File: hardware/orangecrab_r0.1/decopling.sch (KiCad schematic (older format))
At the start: 22 parts

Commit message: Completed 99% of routing.
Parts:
- added C74: 10n, Capacitor_SMD:C_0201_0603Metric, symbol Device:C
- added C75: 100n, Capacitor_SMD:C_0201_0603Metric, symbol Device:C
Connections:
- net GND: now also C74.2, C75.2
- net P3.3V: now also C74.1, C75.1
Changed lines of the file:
@@
 Wire Wire Line
 	4700 4000 4700 4050
+$Comp
+L Device:C C74
+U 1 1 5D761CBE
+P 5600 3800
+F 0 "C74" H 5485 3846 50  0000 R CNN
+F 1 "10n" H 5485 3755 50  0000 R CNN
+F 2 "Capacitor_SMD:C_0201_0603Metric" H 5638 3650 50  0001 C CNN
+F 3 "~" H 5600 3800 50  0001 C CNN
+	1    5600 3800
+	1    0    0    -1
+$EndComp
+$Comp
+L gkl_power:GND #PWR0163
+U 1 1 5D761CC8
+P 5600 4050
+F 0 "#PWR0163" H 5600 3800 50  0001 C CNN
+F 1 "GND" H 5603 3924 50  0000 C CNN
+F 2 "" H 5500 3700 50  0001 C CNN
+F 3 "" H 5600 4050 50  0001 C CNN
+	1    5600 4050
+	1    0    0    -1
+$EndComp
+$Comp
+L Device:C C75
+U 1 1 5D761CD2
+P 5800 3800
+F 0 "C75" H 5915 3846 50  0000 L CNN
+F 1 "100n" H 5915 3755 50  0000 L CNN
+F 2 "Capacitor_SMD:C_0201_0603Metric" H 5838 3650 50  0001 C CNN
+F 3 "~" H 5800 3800 50  0001 C CNN
+	1    5800 3800
+	1    0    0    -1
+$EndComp
+Text GLabel 5800 3550 1    50   UnSpc ~ 0
+P3.3V
+Wire Wire Line
+	5600 3650 5600 3600
+Wire Wire Line
+	5600 3600 5800 3600
+Wire Wire Line
+	5800 3600 5800 3550
+Wire Wire Line
+	5800 3650 5800 3600
+Connection ~ 5800 3600
+Wire Wire Line
+	5600 3950 5600 4000
+Wire Wire Line
+	5600 4000 5800 4000
+Wire Wire Line
+	5800 4000 5800 3950
+Connection ~ 5600 4000
+Wire Wire Line
+	5600 4000 5600 4050
 $EndSCHEMATC

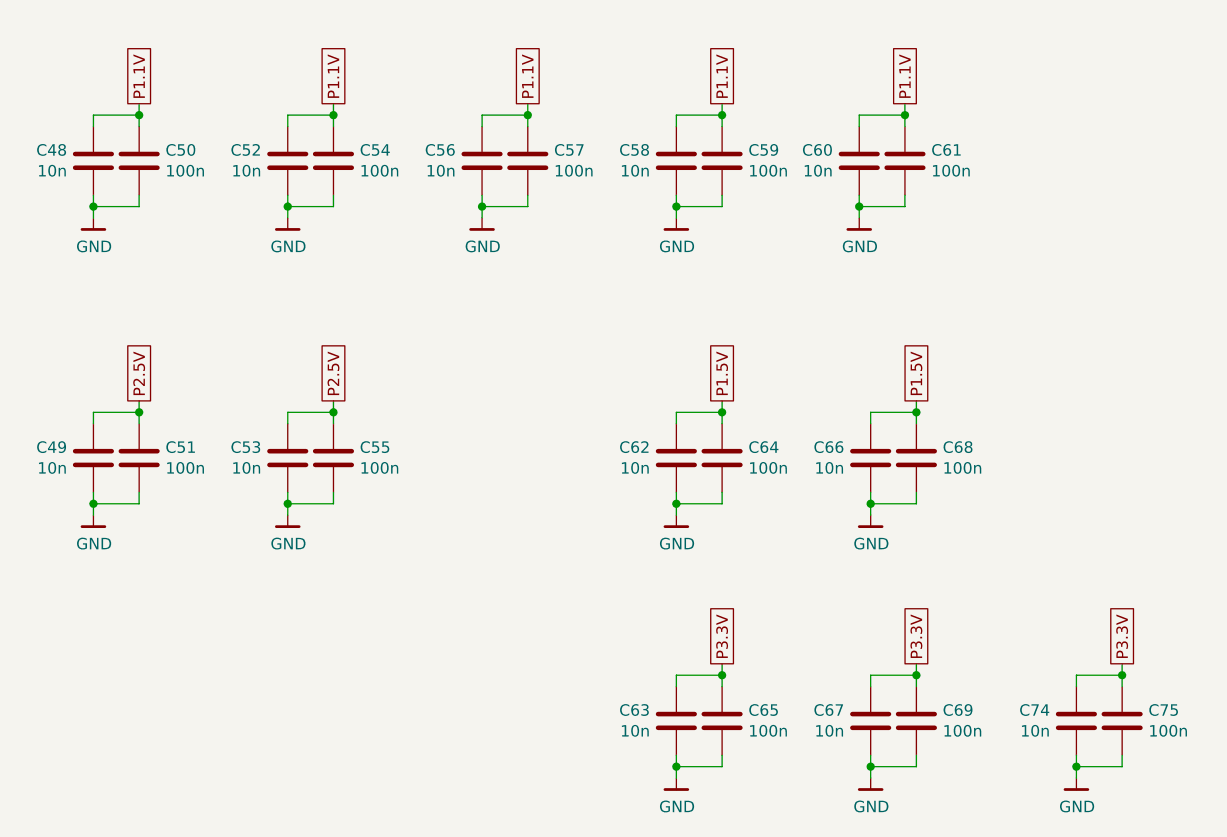
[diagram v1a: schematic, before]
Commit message: Added pulldown on TS pin to disable TS func. Added 4.7uF cap to USB input. Corrected Battery polarity Calculated correct DCDC Fb Added pullup to SWCLK Added Pulldown to TCK Added Pinout legend on top layer Fixed Missing VCC on Flash Neaten up Power Plane Schematic Checklist complete.
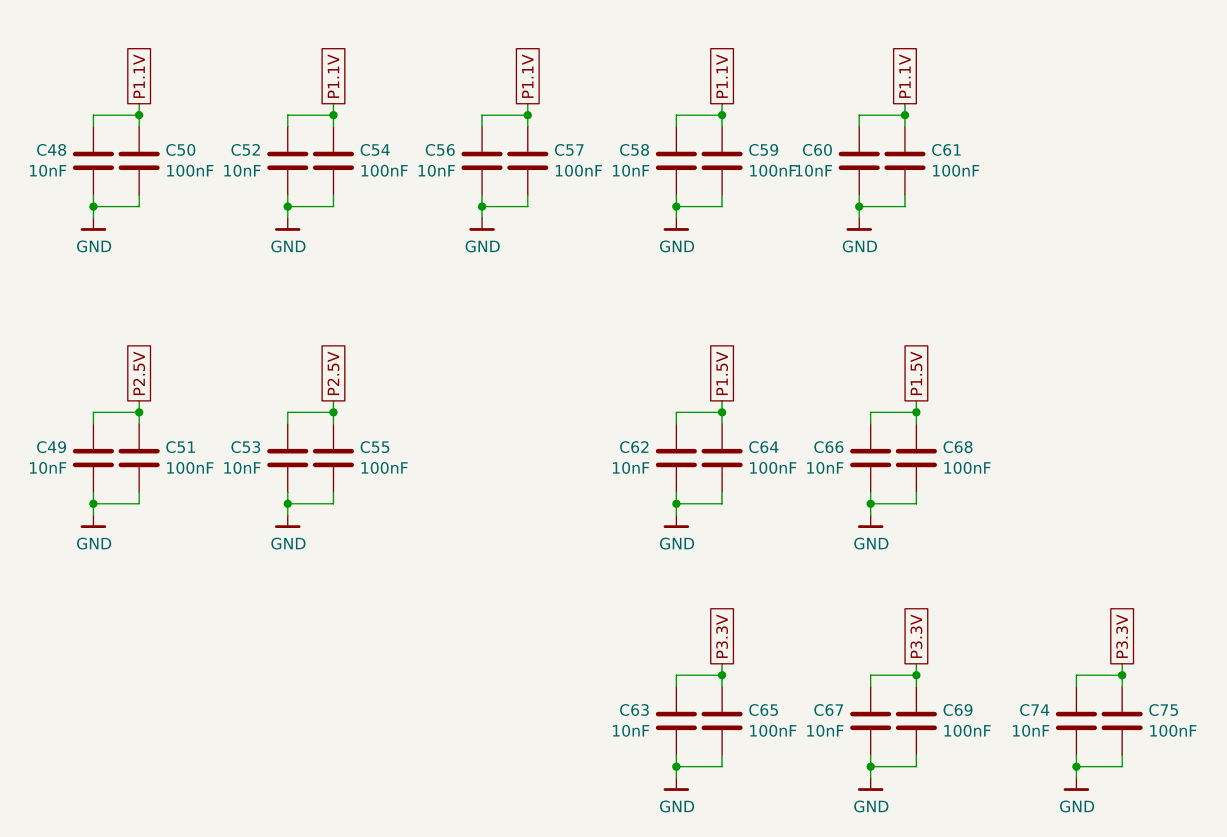
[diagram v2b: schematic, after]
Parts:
- C48, C49, C52, C53, C56, C58, C60, C62, C63, C66, C67, C74: value 10n -> 10nF
- C50, C51, C54, C55, C57, C59, C61, C64, C65, C68, C69, C75: value 100n -> 100nF
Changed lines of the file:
@@
 P 1300 1350
 F 0 "C48" H 1185 1396 50  0000 R CNN
-F 1 "10n" H 1185 1305 50  0000 R CNN
+F 1 "10nF" H 1185 1305 50  0000 R CNN
 F 2 "Capacitor_SMD:C_0201_0603Metric" H 1338 1200 50  0001 C CNN
 F 3 "~" H 1300 1350 50  0001 C CNN
@@
 P 1500 1350
 F 0 "C50" H 1615 1396 50  0000 L CNN
-F 1 "100n" H 1615 1305 50  0000 L CNN
+F 1 "100nF" H 1615 1305 50  0000 L CNN
 F 2 "Capacitor_SMD:C_0201_0603Metric" H 1538 1200 50  0001 C CNN
 F 3 "~" H 1500 1350 50  0001 C CNN
@@
 P 2150 1350
 F 0 "C52" H 2035 1396 50  0000 R CNN
-F 1 "10n" H 2035 1305 50  0000 R CNN
+F 1 "10nF" H 2035 1305 50  0000 R CNN
 F 2 "Capacitor_SMD:C_0201_0603Metric" H 2188 1200 50  0001 C CNN
 F 3 "~" H 2150 1350 50  0001 C CNN
@@
 P 2350 1350
 F 0 "C54" H 2465 1396 50  0000 L CNN
-F 1 "100n" H 2465 1305 50  0000 L CNN
+F 1 "100nF" H 2465 1305 50  0000 L CNN
 F 2 "Capacitor_SMD:C_0201_0603Metric" H 2388 1200 50  0001 C CNN
 F 3 "~" H 2350 1350 50  0001 C CNN
@@
 P 3000 1350
 F 0 "C56" H 2885 1396 50  0000 R CNN
-F 1 "10n" H 2885 1305 50  0000 R CNN
+F 1 "10nF" H 2885 1305 50  0000 R CNN
 F 2 "Capacitor_SMD:C_0201_0603Metric" H 3038 1200 50  0001 C CNN
 F 3 "~" H 3000 1350 50  0001 C CNN
@@
 P 3200 1350
 F 0 "C57" H 3315 1396 50  0000 L CNN
-F 1 "100n" H 3315 1305 50  0000 L CNN
+F 1 "100nF" H 3315 1305 50  0000 L CNN
 F 2 "Capacitor_SMD:C_0201_0603Metric" H 3238 1200 50  0001 C CNN
 F 3 "~" H 3200 1350 50  0001 C CNN
@@
 P 3850 1350
 F 0 "C58" H 3735 1396 50  0000 R CNN
-F 1 "10n" H 3735 1305 50  0000 R CNN
+F 1 "10nF" H 3735 1305 50  0000 R CNN
 F 2 "Capacitor_SMD:C_0201_0603Metric" H 3888 1200 50  0001 C CNN
 F 3 "~" H 3850 1350 50  0001 C CNN
@@
 P 4050 1350
 F 0 "C59" H 4165 1396 50  0000 L CNN
-F 1 "100n" H 4165 1305 50  0000 L CNN
+F 1 "100nF" H 4165 1305 50  0000 L CNN
 F 2 "Capacitor_SMD:C_0201_0603Metric" H 4088 1200 50  0001 C CNN
 F 3 "~" H 4050 1350 50  0001 C CNN
@@
 P 4650 1350
 F 0 "C60" H 4535 1396 50  0000 R CNN
-F 1 "10n" H 4535 1305 50  0000 R CNN
+F 1 "10nF" H 4535 1305 50  0000 R CNN
 F 2 "Capacitor_SMD:C_0201_0603Metric" H 4688 1200 50  0001 C CNN
 F 3 "~" H 4650 1350 50  0001 C CNN
@@
 P 4850 1350
 F 0 "C61" H 4965 1396 50  0000 L CNN
-F 1 "100n" H 4965 1305 50  0000 L CNN
+F 1 "100nF" H 4965 1305 50  0000 L CNN
 F 2 "Capacitor_SMD:C_0201_0603Metric" H 4888 1200 50  0001 C CNN
 F 3 "~" H 4850 1350 50  0001 C CNN
@@
 P 1300 2650
 F 0 "C49" H 1185 2696 50  0000 R CNN
-F 1 "10n" H 1185 2605 50  0000 R CNN
+F 1 "10nF" H 1185 2605 50  0000 R CNN
 F 2 "Capacitor_SMD:C_0201_0603Metric" H 1338 2500 50  0001 C CNN
 F 3 "~" H 1300 2650 50  0001 C CNN
@@
 P 1500 2650
 F 0 "C51" H 1615 2696 50  0000 L CNN
-F 1 "100n" H 1615 2605 50  0000 L CNN
+F 1 "100nF" H 1615 2605 50  0000 L CNN
 F 2 "Capacitor_SMD:C_0201_0603Metric" H 1538 2500 50  0001 C CNN
 F 3 "~" H 1500 2650 50  0001 C CNN
@@
 P 2150 2650
 F 0 "C53" H 2035 2696 50  0000 R CNN
-F 1 "10n" H 2035 2605 50  0000 R CNN
+F 1 "10nF" H 2035 2605 50  0000 R CNN
 F 2 "Capacitor_SMD:C_0201_0603Metric" H 2188 2500 50  0001 C CNN
 F 3 "~" H 2150 2650 50  0001 C CNN
@@
 P 2350 2650
 F 0 "C55" H 2465 2696 50  0000 L CNN
-F 1 "100n" H 2465 2605 50  0000 L CNN
+F 1 "100nF" H 2465 2605 50  0000 L CNN
 F 2 "Capacitor_SMD:C_0201_0603Metric" H 2388 2500 50  0001 C CNN
 F 3 "~" H 2350 2650 50  0001 C CNN
@@
 P 3850 2650
 F 0 "C62" H 3735 2696 50  0000 R CNN
-F 1 "10n" H 3735 2605 50  0000 R CNN
+F 1 "10nF" H 3735 2605 50  0000 R CNN
 F 2 "Capacitor_SMD:C_0201_0603Metric" H 3888 2500 50  0001 C CNN
 F 3 "~" H 3850 2650 50  0001 C CNN
@@
 P 4050 2650
 F 0 "C64" H 4165 2696 50  0000 L CNN
-F 1 "100n" H 4165 2605 50  0000 L CNN
+F 1 "100nF" H 4165 2605 50  0000 L CNN
 F 2 "Capacitor_SMD:C_0201_0603Metric" H 4088 2500 50  0001 C CNN
 F 3 "~" H 4050 2650 50  0001 C CNN
@@
 P 4700 2650
 F 0 "C66" H 4585 2696 50  0000 R CNN
-F 1 "10n" H 4585 2605 50  0000 R CNN
+F 1 "10nF" H 4585 2605 50  0000 R CNN
 F 2 "Capacitor_SMD:C_0201_0603Metric" H 4738 2500 50  0001 C CNN
 F 3 "~" H 4700 2650 50  0001 C CNN
@@
 P 4900 2650
 F 0 "C68" H 5015 2696 50  0000 L CNN
-F 1 "100n" H 5015 2605 50  0000 L CNN
+F 1 "100nF" H 5015 2605 50  0000 L CNN
 F 2 "Capacitor_SMD:C_0201_0603Metric" H 4938 2500 50  0001 C CNN
 F 3 "~" H 4900 2650 50  0001 C CNN
@@
 P 3850 3800
 F 0 "C63" H 3735 3846 50  0000 R CNN
-F 1 "10n" H 3735 3755 50  0000 R CNN
+F 1 "10nF" H 3735 3755 50  0000 R CNN
 F 2 "Capacitor_SMD:C_0201_0603Metric" H 3888 3650 50  0001 C CNN
 F 3 "~" H 3850 3800 50  0001 C CNN
@@
 P 4050 3800
 F 0 "C65" H 4165 3846 50  0000 L CNN
-F 1 "100n" H 4165 3755 50  0000 L CNN
+F 1 "100nF" H 4165 3755 50  0000 L CNN
 F 2 "Capacitor_SMD:C_0201_0603Metric" H 4088 3650 50  0001 C CNN
 F 3 "~" H 4050 3800 50  0001 C CNN
@@
 P 4700 3800
 F 0 "C67" H 4585 3846 50  0000 R CNN
-F 1 "10n" H 4585 3755 50  0000 R CNN
+F 1 "10nF" H 4585 3755 50  0000 R CNN
 F 2 "Capacitor_SMD:C_0201_0603Metric" H 4738 3650 50  0001 C CNN
 F 3 "~" H 4700 3800 50  0001 C CNN
@@
 P 4900 3800
 F 0 "C69" H 5015 3846 50  0000 L CNN
-F 1 "100n" H 5015 3755 50  0000 L CNN
+F 1 "100nF" H 5015 3755 50  0000 L CNN
 F 2 "Capacitor_SMD:C_0201_0603Metric" H 4938 3650 50  0001 C CNN
 F 3 "~" H 4900 3800 50  0001 C CNN
@@
 P 5600 3800
 F 0 "C74" H 5485 3846 50  0000 R CNN
-F 1 "10n" H 5485 3755 50  0000 R CNN
+F 1 "10nF" H 5485 3755 50  0000 R CNN
 F 2 "Capacitor_SMD:C_0201_0603Metric" H 5638 3650 50  0001 C CNN
 F 3 "~" H 5600 3800 50  0001 C CNN
@@
 P 5800 3800
 F 0 "C75" H 5915 3846 50  0000 L CNN
-F 1 "100n" H 5915 3755 50  0000 L CNN
+F 1 "100nF" H 5915 3755 50  0000 L CNN
 F 2 "Capacitor_SMD:C_0201_0603Metric" H 5838 3650 50  0001 C CNN
 F 3 "~" H 5800 3800 50  0001 C CNN

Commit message: Updated BOM fields in KiCad project Exported ibom Clarify fab notes
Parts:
- C48, C49, C52, C53, C56, C58, C60, C62, C63, C66, C67, C74: Mfg (none) -> Samsung Electro-Mechanics; PN (none) -> CL03B103KP3NNNC
- C50, C51, C54, C55, C57, C59, C61, C64, C65, C68, C69, C75: Mfg (none) -> Samsung Electro-Mechanics; PN (none) -> CL03A104KQ3NNNC
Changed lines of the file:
@@
 F 2 "Capacitor_SMD:C_0201_0603Metric" H 1338 1200 50  0001 C CNN
 F 3 "~" H 1300 1350 50  0001 C CNN
+F 4 "Samsung Electro-Mechanics" H 1300 1350 50  0001 C CNN "Mfg"
+F 5 "CL03B103KP3NNNC" H 1300 1350 50  0001 C CNN "PN"
 	1    1300 1350
 	1    0    0    -1
@@
 F 2 "Capacitor_SMD:C_0201_0603Metric" H 1538 1200 50  0001 C CNN
 F 3 "~" H 1500 1350 50  0001 C CNN
+F 4 "Samsung Electro-Mechanics" H 1500 1350 50  0001 C CNN "Mfg"
+F 5 "CL03A104KQ3NNNC" H 1500 1350 50  0001 C CNN "PN"
 	1    1500 1350
 	1    0    0    -1
@@
 F 2 "Capacitor_SMD:C_0201_0603Metric" H 2188 1200 50  0001 C CNN
 F 3 "~" H 2150 1350 50  0001 C CNN
+F 4 "Samsung Electro-Mechanics" H 2150 1350 50  0001 C CNN "Mfg"
+F 5 "CL03B103KP3NNNC" H 2150 1350 50  0001 C CNN "PN"
 	1    2150 1350
 	1    0    0    -1
@@
 F 2 "Capacitor_SMD:C_0201_0603Metric" H 2388 1200 50  0001 C CNN
 F 3 "~" H 2350 1350 50  0001 C CNN
+F 4 "Samsung Electro-Mechanics" H 2350 1350 50  0001 C CNN "Mfg"
+F 5 "CL03A104KQ3NNNC" H 2350 1350 50  0001 C CNN "PN"
 	1    2350 1350
 	1    0    0    -1
@@
 F 2 "Capacitor_SMD:C_0201_0603Metric" H 3038 1200 50  0001 C CNN
 F 3 "~" H 3000 1350 50  0001 C CNN
+F 4 "Samsung Electro-Mechanics" H 3000 1350 50  0001 C CNN "Mfg"
+F 5 "CL03B103KP3NNNC" H 3000 1350 50  0001 C CNN "PN"
 	1    3000 1350
 	1    0    0    -1
@@
 F 2 "Capacitor_SMD:C_0201_0603Metric" H 3238 1200 50  0001 C CNN
 F 3 "~" H 3200 1350 50  0001 C CNN
+F 4 "Samsung Electro-Mechanics" H 3200 1350 50  0001 C CNN "Mfg"
+F 5 "CL03A104KQ3NNNC" H 3200 1350 50  0001 C CNN "PN"
 	1    3200 1350
 	1    0    0    -1
@@
 F 2 "Capacitor_SMD:C_0201_0603Metric" H 3888 1200 50  0001 C CNN
 F 3 "~" H 3850 1350 50  0001 C CNN
+F 4 "Samsung Electro-Mechanics" H 3850 1350 50  0001 C CNN "Mfg"
+F 5 "CL03B103KP3NNNC" H 3850 1350 50  0001 C CNN "PN"
 	1    3850 1350
 	1    0    0    -1
@@
 F 2 "Capacitor_SMD:C_0201_0603Metric" H 4088 1200 50  0001 C CNN
 F 3 "~" H 4050 1350 50  0001 C CNN
+F 4 "Samsung Electro-Mechanics" H 4050 1350 50  0001 C CNN "Mfg"
+F 5 "CL03A104KQ3NNNC" H 4050 1350 50  0001 C CNN "PN"
 	1    4050 1350
 	1    0    0    -1
@@
 F 2 "Capacitor_SMD:C_0201_0603Metric" H 4688 1200 50  0001 C CNN
 F 3 "~" H 4650 1350 50  0001 C CNN
+F 4 "Samsung Electro-Mechanics" H 4650 1350 50  0001 C CNN "Mfg"
+F 5 "CL03B103KP3NNNC" H 4650 1350 50  0001 C CNN "PN"
 	1    4650 1350
 	1    0    0    -1
@@
 F 2 "Capacitor_SMD:C_0201_0603Metric" H 4888 1200 50  0001 C CNN
 F 3 "~" H 4850 1350 50  0001 C CNN
+F 4 "Samsung Electro-Mechanics" H 4850 1350 50  0001 C CNN "Mfg"
+F 5 "CL03A104KQ3NNNC" H 4850 1350 50  0001 C CNN "PN"
 	1    4850 1350
 	1    0    0    -1
@@
 F 2 "Capacitor_SMD:C_0201_0603Metric" H 1338 2500 50  0001 C CNN
 F 3 "~" H 1300 2650 50  0001 C CNN
+F 4 "Samsung Electro-Mechanics" H 1300 2650 50  0001 C CNN "Mfg"
+F 5 "CL03B103KP3NNNC" H 1300 2650 50  0001 C CNN "PN"
 	1    1300 2650
 	1    0    0    -1
@@
 F 2 "Capacitor_SMD:C_0201_0603Metric" H 1538 2500 50  0001 C CNN
 F 3 "~" H 1500 2650 50  0001 C CNN
+F 4 "Samsung Electro-Mechanics" H 1500 2650 50  0001 C CNN "Mfg"
+F 5 "CL03A104KQ3NNNC" H 1500 2650 50  0001 C CNN "PN"
 	1    1500 2650
 	1    0    0    -1
@@
 F 2 "Capacitor_SMD:C_0201_0603Metric" H 2188 2500 50  0001 C CNN
 F 3 "~" H 2150 2650 50  0001 C CNN
+F 4 "Samsung Electro-Mechanics" H 2150 2650 50  0001 C CNN "Mfg"
+F 5 "CL03B103KP3NNNC" H 2150 2650 50  0001 C CNN "PN"
 	1    2150 2650
 	1    0    0    -1
@@
 F 2 "Capacitor_SMD:C_0201_0603Metric" H 2388 2500 50  0001 C CNN
 F 3 "~" H 2350 2650 50  0001 C CNN
+F 4 "Samsung Electro-Mechanics" H 2350 2650 50  0001 C CNN "Mfg"
+F 5 "CL03A104KQ3NNNC" H 2350 2650 50  0001 C CNN "PN"
 	1    2350 2650
 	1    0    0    -1
@@
 F 2 "Capacitor_SMD:C_0201_0603Metric" H 3888 2500 50  0001 C CNN
 F 3 "~" H 3850 2650 50  0001 C CNN
+F 4 "Samsung Electro-Mechanics" H 3850 2650 50  0001 C CNN "Mfg"
+F 5 "CL03B103KP3NNNC" H 3850 2650 50  0001 C CNN "PN"
 	1    3850 2650
 	1    0    0    -1
@@
 F 2 "Capacitor_SMD:C_0201_0603Metric" H 4088 2500 50  0001 C CNN
 F 3 "~" H 4050 2650 50  0001 C CNN
+F 4 "Samsung Electro-Mechanics" H 4050 2650 50  0001 C CNN "Mfg"
+F 5 "CL03A104KQ3NNNC" H 4050 2650 50  0001 C CNN "PN"
 	1    4050 2650
 	1    0    0    -1
@@
 F 2 "Capacitor_SMD:C_0201_0603Metric" H 4738 2500 50  0001 C CNN
 F 3 "~" H 4700 2650 50  0001 C CNN
+F 4 "Samsung Electro-Mechanics" H 4700 2650 50  0001 C CNN "Mfg"
+F 5 "CL03B103KP3NNNC" H 4700 2650 50  0001 C CNN "PN"
 	1    4700 2650
 	1    0    0    -1
@@
 F 2 "Capacitor_SMD:C_0201_0603Metric" H 4938 2500 50  0001 C CNN
 F 3 "~" H 4900 2650 50  0001 C CNN
+F 4 "Samsung Electro-Mechanics" H 4900 2650 50  0001 C CNN "Mfg"
+F 5 "CL03A104KQ3NNNC" H 4900 2650 50  0001 C CNN "PN"
 	1    4900 2650
 	1    0    0    -1
@@
 F 2 "Capacitor_SMD:C_0201_0603Metric" H 3888 3650 50  0001 C CNN
 F 3 "~" H 3850 3800 50  0001 C CNN
+F 4 "Samsung Electro-Mechanics" H 3850 3800 50  0001 C CNN "Mfg"
+F 5 "CL03B103KP3NNNC" H 3850 3800 50  0001 C CNN "PN"
 	1    3850 3800
 	1    0    0    -1
@@
 F 2 "Capacitor_SMD:C_0201_0603Metric" H 4088 3650 50  0001 C CNN
 F 3 "~" H 4050 3800 50  0001 C CNN
+F 4 "Samsung Electro-Mechanics" H 4050 3800 50  0001 C CNN "Mfg"
+F 5 "CL03A104KQ3NNNC" H 4050 3800 50  0001 C CNN "PN"
 	1    4050 3800
 	1    0    0    -1
@@
 F 2 "Capacitor_SMD:C_0201_0603Metric" H 4738 3650 50  0001 C CNN
 F 3 "~" H 4700 3800 50  0001 C CNN
+F 4 "Samsung Electro-Mechanics" H 4700 3800 50  0001 C CNN "Mfg"
+F 5 "CL03B103KP3NNNC" H 4700 3800 50  0001 C CNN "PN"
 	1    4700 3800
 	1    0    0    -1
@@
 F 2 "Capacitor_SMD:C_0201_0603Metric" H 4938 3650 50  0001 C CNN
 F 3 "~" H 4900 3800 50  0001 C CNN
+F 4 "Samsung Electro-Mechanics" H 4900 3800 50  0001 C CNN "Mfg"
+F 5 "CL03A104KQ3NNNC" H 4900 3800 50  0001 C CNN "PN"
 	1    4900 3800
 	1    0    0    -1
@@
 F 2 "Capacitor_SMD:C_0201_0603Metric" H 5638 3650 50  0001 C CNN
 F 3 "~" H 5600 3800 50  0001 C CNN
+F 4 "Samsung Electro-Mechanics" H 5600 3800 50  0001 C CNN "Mfg"
+F 5 "CL03B103KP3NNNC" H 5600 3800 50  0001 C CNN "PN"
 	1    5600 3800
 	1    0    0    -1
@@
 F 2 "Capacitor_SMD:C_0201_0603Metric" H 5838 3650 50  0001 C CNN
 F 3 "~" H 5800 3800 50  0001 C CNN
+F 4 "Samsung Electro-Mechanics" H 5800 3800 50  0001 C CNN "Mfg"
+F 5 "CL03A104KQ3NNNC" H 5800 3800 50  0001 C CNN "PN"
 	1    5800 3800
 	1    0    0    -1

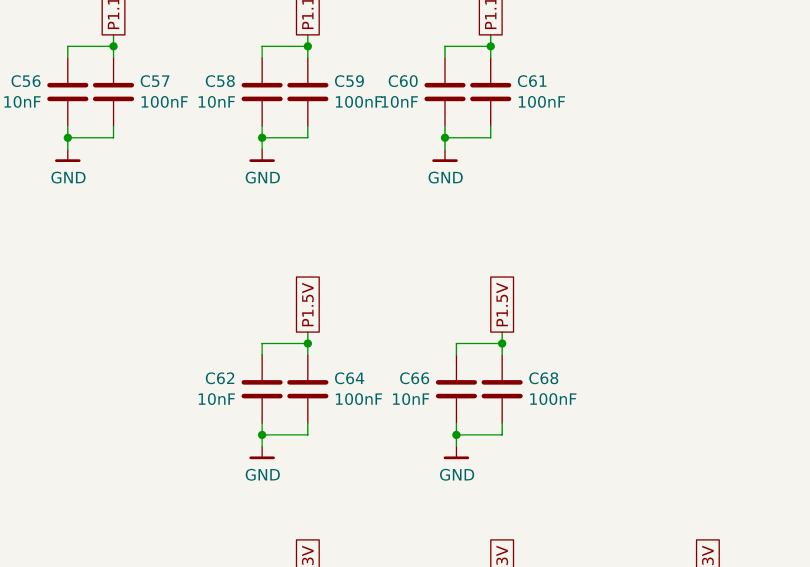
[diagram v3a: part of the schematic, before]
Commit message: r0.1 PCB: Switch P1.5 to P1.35V
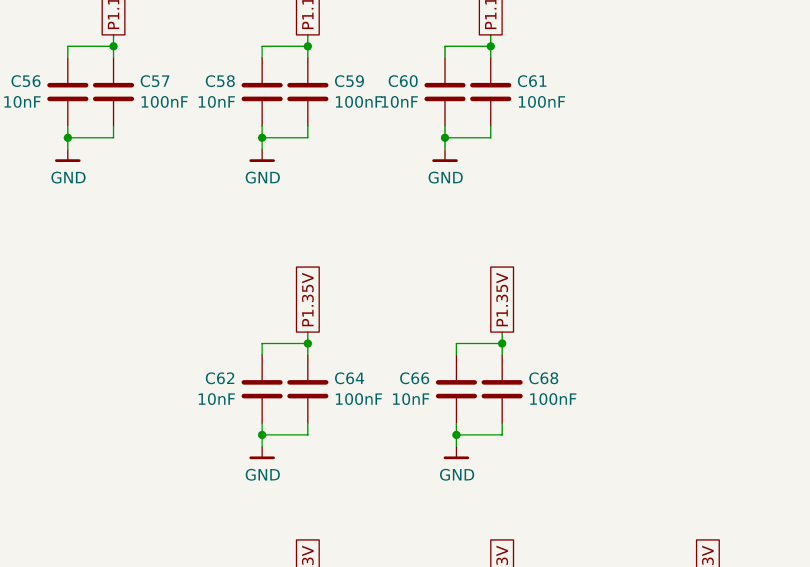
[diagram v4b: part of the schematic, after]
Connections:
- net P1.5V renamed P1.35V
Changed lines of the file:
@@
 EESchema Schematic File Version 4
 LIBS:OrangeCrab-cache
-EELAYER 29 0
+EELAYER 30 0
 EELAYER END
 $Descr A4 11693 8268
@@
 $EndComp
 Text GLabel 4050 2400 1    50   UnSpc ~ 0
-P1.5V
+P1.35V
 Wire Wire Line
 	3850 2500 3850 2450
@@
 $EndComp
 Text GLabel 4900 2400 1    50   UnSpc ~ 0
-P1.5V
+P1.35V
 Wire Wire Line
 	4700 2500 4700 2450
